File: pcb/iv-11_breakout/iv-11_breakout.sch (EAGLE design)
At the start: 2 parts

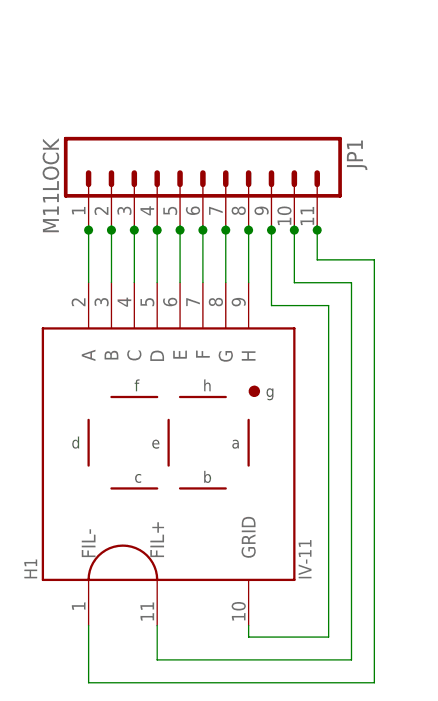
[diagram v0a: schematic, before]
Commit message: New layout for the IV-11 breakout, fixed the drill size
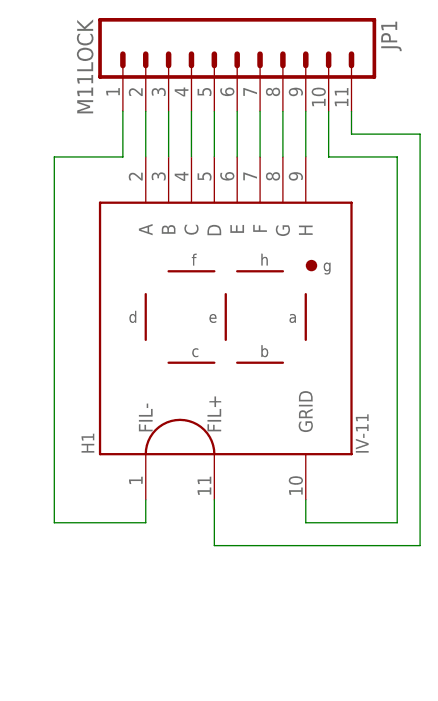
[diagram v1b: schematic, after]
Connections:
- net N$1: now also JP1.2; no longer JP1.1
- net N$10: now also H1.GRID; no longer H1.FIL+
- net N$11: now also H1.FIL+; no longer H1.FIL-
- net N$2: now also JP1.3; no longer JP1.2
- net N$3: now also JP1.4; no longer JP1.3
- net N$4: now also JP1.5; no longer JP1.4
- net N$5: now also JP1.6; no longer JP1.5
- net N$6: now also JP1.7; no longer JP1.6
- net N$7: now also JP1.8; no longer JP1.7
- net N$8: now also JP1.9; no longer JP1.8
- net N$9: now also H1.FIL-, JP1.1; no longer H1.GRID, JP1.9
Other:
- moved on the sheet: H1, JP1
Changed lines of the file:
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@@
 </plain>
 <instances>
-<instance part="JP1" gate="G$1" x="24.13" y="62.992" rot="R270"/>
-<instance part="H1" gate="G$1" x="20.32" y="29.21"/>
+<instance part="JP1" gate="G$1" x="27.94" y="76.2" rot="R270"/>
+<instance part="H1" gate="G$1" x="27.94" y="43.18"/>
 </instances>
 <busses>
@@
 <net name="N$1" class="0">
 <segment>
-<wire x1="11.43" y1="53.34" x2="11.43" y2="52.832" width="0.1524" layer="91"/>
-<pinref part="JP1" gate="G$1" pin="1"/>
-<wire x1="11.43" y1="52.832" x2="11.43" y2="46.99" width="0.1524" layer="91"/>
-<junction x="11.43" y="52.832"/>
 <pinref part="H1" gate="G$1" pin="A"/>
+<pinref part="JP1" gate="G$1" pin="2"/>
+<wire x1="17.78" y1="60.96" x2="17.78" y2="66.04" width="0.1524" layer="91"/>
 </segment>
 </net>
 <net name="N$2" class="0">
 <segment>
-<wire x1="13.97" y1="46.99" x2="13.97" y2="52.832" width="0.1524" layer="91"/>
-<pinref part="JP1" gate="G$1" pin="2"/>
-<wire x1="13.97" y1="52.832" x2="13.97" y2="53.34" width="0.1524" layer="91"/>
-<junction x="13.97" y="52.832"/>
+<pinref part="JP1" gate="G$1" pin="3"/>
 <pinref part="H1" gate="G$1" pin="B"/>
+<wire x1="20.32" y1="66.04" x2="20.32" y2="60.96" width="0.1524" layer="91"/>
 </segment>
 </net>
 <net name="N$3" class="0">
 <segment>
-<wire x1="16.51" y1="53.34" x2="16.51" y2="52.832" width="0.1524" layer="91"/>
-<pinref part="JP1" gate="G$1" pin="3"/>
-<wire x1="16.51" y1="52.832" x2="16.51" y2="46.99" width="0.1524" layer="91"/>
-<junction x="16.51" y="52.832"/>
 <pinref part="H1" gate="G$1" pin="C"/>
+<pinref part="JP1" gate="G$1" pin="4"/>
+<wire x1="22.86" y1="60.96" x2="22.86" y2="66.04" width="0.1524" layer="91"/>
 </segment>
 </net>
 <net name="N$4" class="0">
 <segment>
-<wire x1="19.05" y1="46.99" x2="19.05" y2="52.832" width="0.1524" layer="91"/>
-<pinref part="JP1" gate="G$1" pin="4"/>
-<wire x1="19.05" y1="52.832" x2="19.05" y2="53.34" width="0.1524" layer="91"/>
-<junction x="19.05" y="52.832"/>
+<pinref part="JP1" gate="G$1" pin="5"/>
 <pinref part="H1" gate="G$1" pin="D"/>
+<wire x1="25.4" y1="66.04" x2="25.4" y2="60.96" width="0.1524" layer="91"/>
 </segment>
 </net>
 <net name="N$5" class="0">
 <segment>
-<wire x1="21.59" y1="53.34" x2="21.59" y2="52.832" width="0.1524" layer="91"/>
-<pinref part="JP1" gate="G$1" pin="5"/>
-<wire x1="21.59" y1="52.832" x2="21.59" y2="46.99" width="0.1524" layer="91"/>
-<junction x="21.59" y="52.832"/>
 <pinref part="H1" gate="G$1" pin="E"/>
+<pinref part="JP1" gate="G$1" pin="6"/>
+<wire x1="27.94" y1="60.96" x2="27.94" y2="66.04" width="0.1524" layer="91"/>
 </segment>
 </net>
 <net name="N$6" class="0">
 <segment>
-<wire x1="24.13" y1="46.99" x2="24.13" y2="52.832" width="0.1524" layer="91"/>
-<pinref part="JP1" gate="G$1" pin="6"/>
-<wire x1="24.13" y1="52.832" x2="24.13" y2="53.34" width="0.1524" layer="91"/>
-<junction x="24.13" y="52.832"/>
+<pinref part="JP1" gate="G$1" pin="7"/>
 <pinref part="H1" gate="G$1" pin="F"/>
+<wire x1="30.48" y1="66.04" x2="30.48" y2="60.96" width="0.1524" layer="91"/>
 </segment>
 </net>
 <net name="N$7" class="0">
 <segment>
-<wire x1="26.67" y1="53.34" x2="26.67" y2="52.832" width="0.1524" layer="91"/>
-<pinref part="JP1" gate="G$1" pin="7"/>
-<wire x1="26.67" y1="52.832" x2="26.67" y2="46.99" width="0.1524" layer="91"/>
-<junction x="26.67" y="52.832"/>
 <pinref part="H1" gate="G$1" pin="G"/>
+<pinref part="JP1" gate="G$1" pin="8"/>
+<wire x1="33.02" y1="60.96" x2="33.02" y2="66.04" width="0.1524" layer="91"/>
 </segment>
 </net>
 <net name="N$8" class="0">
 <segment>
-<wire x1="29.21" y1="46.99" x2="29.21" y2="52.832" width="0.1524" layer="91"/>
-<pinref part="JP1" gate="G$1" pin="8"/>
-<wire x1="29.21" y1="52.832" x2="29.21" y2="53.34" width="0.1524" layer="91"/>
-<junction x="29.21" y="52.832"/>
+<pinref part="JP1" gate="G$1" pin="9"/>
 <pinref part="H1" gate="G$1" pin="H"/>
+<wire x1="35.56" y1="66.04" x2="35.56" y2="60.96" width="0.1524" layer="91"/>
 </segment>
 </net>
 <net name="N$9" class="0">
 <segment>
-<wire x1="29.21" y1="8.89" x2="29.21" y2="7.62" width="0.1524" layer="91"/>
-<wire x1="29.21" y1="7.62" x2="38.1" y2="7.62" width="0.1524" layer="91"/>
-<wire x1="38.1" y1="7.62" x2="38.1" y2="44.45" width="0.1524" layer="91"/>
-<wire x1="38.1" y1="44.45" x2="31.75" y2="44.45" width="0.1524" layer="91"/>
-<wire x1="31.75" y1="44.45" x2="31.75" y2="52.832" width="0.1524" layer="91"/>
-<pinref part="JP1" gate="G$1" pin="9"/>
-<wire x1="31.75" y1="52.832" x2="31.75" y2="53.34" width="0.1524" layer="91"/>
-<junction x="31.75" y="52.832"/>
-<pinref part="H1" gate="G$1" pin="GRID"/>
+<pinref part="JP1" gate="G$1" pin="1"/>
+<wire x1="15.24" y1="66.04" x2="15.24" y2="60.96" width="0.1524" layer="91"/>
+<wire x1="15.24" y1="60.96" x2="7.62" y2="60.96" width="0.1524" layer="91"/>
+<wire x1="7.62" y1="60.96" x2="7.62" y2="20.32" width="0.1524" layer="91"/>
+<pinref part="H1" gate="G$1" pin="FIL-"/>
+<wire x1="7.62" y1="20.32" x2="17.78" y2="20.32" width="0.1524" layer="91"/>
+<wire x1="17.78" y1="20.32" x2="17.78" y2="22.86" width="0.1524" layer="91"/>
 </segment>
 </net>
 <net name="N$10" class="0">
 <segment>
-<wire x1="34.29" y1="53.34" x2="34.29" y2="52.832" width="0.1524" layer="91"/>
-<wire x1="34.29" y1="52.832" x2="34.29" y2="46.99" width="0.1524" layer="91"/>
-<wire x1="34.29" y1="46.99" x2="40.64" y2="46.99" width="0.1524" layer="91"/>
-<wire x1="40.64" y1="46.99" x2="40.64" y2="5.08" width="0.1524" layer="91"/>
-<wire x1="40.64" y1="5.08" x2="19.05" y2="5.08" width="0.1524" layer="91"/>
-<wire x1="19.05" y1="5.08" x2="19.05" y2="8.89" width="0.1524" layer="91"/>
+<pinref part="H1" gate="G$1" pin="GRID"/>
+<wire x1="35.56" y1="22.86" x2="35.56" y2="20.32" width="0.1524" layer="91"/>
+<wire x1="35.56" y1="20.32" x2="45.72" y2="20.32" width="0.1524" layer="91"/>
+<wire x1="45.72" y1="20.32" x2="45.72" y2="60.96" width="0.1524" layer="91"/>
 <pinref part="JP1" gate="G$1" pin="10"/>
-<junction x="34.29" y="52.832"/>
-<pinref part="H1" gate="G$1" pin="FIL+"/>
+<wire x1="45.72" y1="60.96" x2="38.1" y2="60.96" width="0.1524" layer="91"/>
+<wire x1="38.1" y1="60.96" x2="38.1" y2="66.04" width="0.1524" layer="91"/>
 </segment>
 </net>
 <net name="N$11" class="0">
 <segment>
-<wire x1="11.43" y1="8.89" x2="11.43" y2="2.54" width="0.1524" layer="91"/>
-<wire x1="11.43" y1="2.54" x2="43.18" y2="2.54" width="0.1524" layer="91"/>
-<wire x1="43.18" y1="2.54" x2="43.18" y2="49.53" width="0.1524" layer="91"/>
-<wire x1="43.18" y1="49.53" x2="36.83" y2="49.53" width="0.1524" layer="91"/>
-<wire x1="36.83" y1="49.53" x2="36.83" y2="52.832" width="0.1524" layer="91"/>
 <pinref part="JP1" gate="G$1" pin="11"/>
-<wire x1="36.83" y1="52.832" x2="36.83" y2="53.34" width="0.1524" layer="91"/>
-<junction x="36.83" y="52.832"/>
-<pinref part="H1" gate="G$1" pin="FIL-"/>
+<wire x1="40.64" y1="66.04" x2="40.64" y2="63.5" width="0.1524" layer="91"/>
+<wire x1="40.64" y1="63.5" x2="48.26" y2="63.5" width="0.1524" layer="91"/>
+<wire x1="48.26" y1="63.5" x2="48.26" y2="17.78" width="0.1524" layer="91"/>
+<pinref part="H1" gate="G$1" pin="FIL+"/>
+<wire x1="48.26" y1="17.78" x2="25.4" y2="17.78" width="0.1524" layer="91"/>
+<wire x1="25.4" y1="17.78" x2="25.4" y2="22.86" width="0.1524" layer="91"/>
 </segment>
 </net>
